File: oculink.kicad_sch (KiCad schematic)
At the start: 28 parts, among them J4 OCuLink_x4_Amphenol_G14A42121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, U2 MAX3373EEKA+

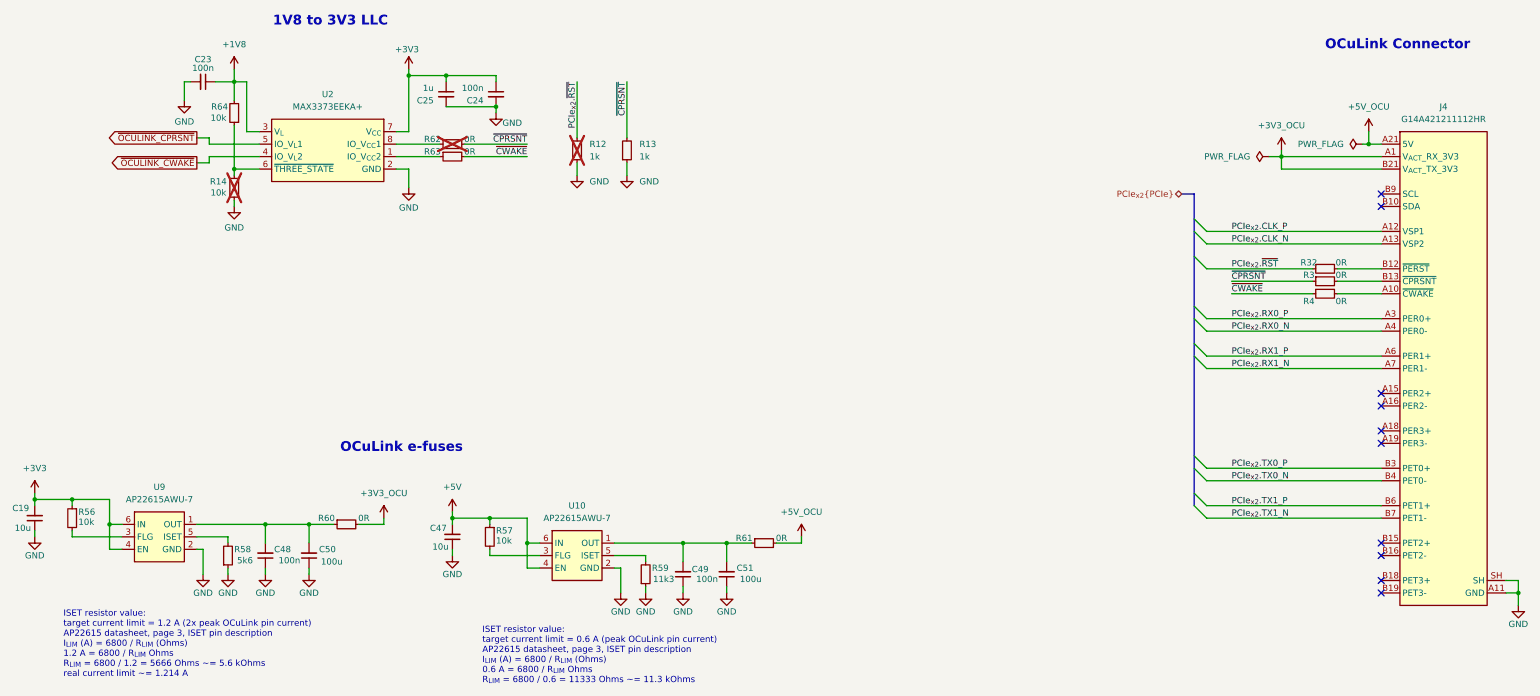
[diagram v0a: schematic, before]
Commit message: [#100765] WIP: Apply review changes
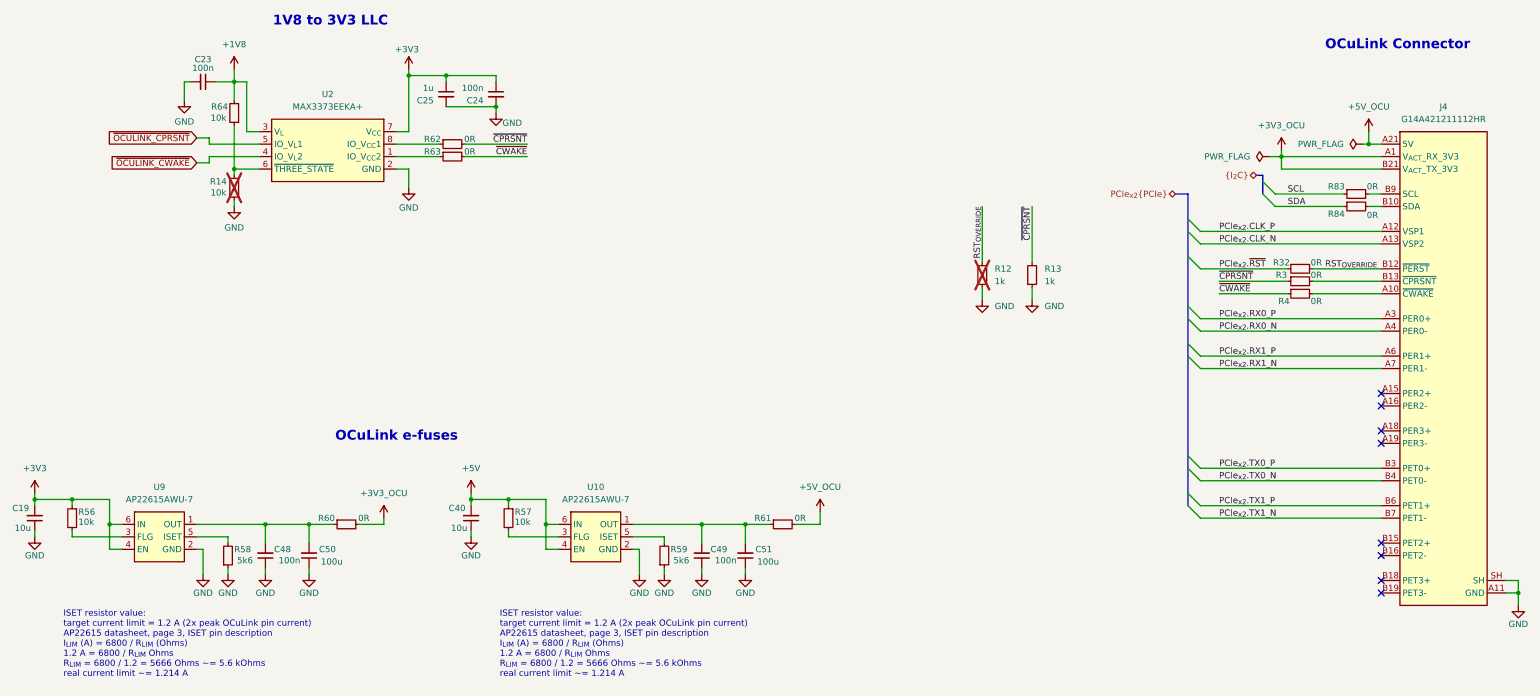
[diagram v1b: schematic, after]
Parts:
- removed C47: C_10u_0402, antmicro-footprints:C_0402_1005Metric, symbol antmicroCapacitors0402:C_10u_0402
- removed R59: R_11k3_0402, antmicro-footprints:R_0402_1005Metric, symbol antmicroResistors0402:R_11k3_0402
- added C40: C_10u_0402, antmicro-footprints:C_0402_1005Metric, symbol antmicroCapacitors0402:C_10u_0402
- added R59: R_5k6_0402, antmicro-footprints:R_0402_1005Metric, symbol antmicroResistors0402:R_5k6_0402
- added R83, R84: R_0R_0402, antmicro-footprints:R_0402_1005Metric, symbol antmicroResistors0402:R_0R_0402
- R62: now fitted
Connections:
- net +5V: now also C40.2
- net GND: now also C40.1, R59.1
- net PCIe_{x2}.~{RST}: no longer R12.2
- net at U10.5 (ISET): now also R59.2
- net RST_{OVERRIDE}: now reaches J4.B12 (~{PERST}), R32.2
- net RST_{OVERRIDE}: now also R12.2
- net at J4.B10 (SDA): now also R84.2
- net at J4.B9 (SCL): now also R83.2
- new net SCL: R83.1
- new net SDA: R84.1
- no-connect marks 10 -> 8
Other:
- note removed: "ISET resistor value: target current limit = 0.6 A (peak OCuLink pin current) AP22615 datasheet, page 3, ISET pin description I_{LIM} (A) = 6800 / R_{LIM} (Ohms) 0.6 A = 6800 / R_{LIM} Ohms R_{LIM} = 6800 / 0.6 = 11333 Ohms ~= 11.3 kOhms"
- moved on the sheet: R12, R13, R3, R32, R4

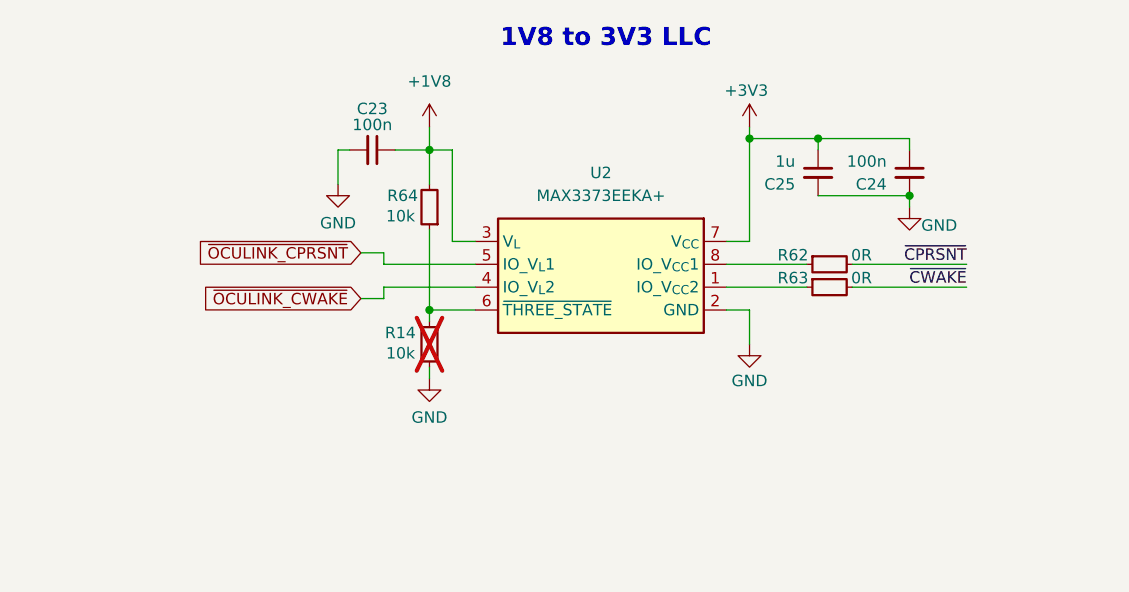
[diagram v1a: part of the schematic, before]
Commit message: [#100765] Change MAX3373EEKA+ to NTS0302JKZ
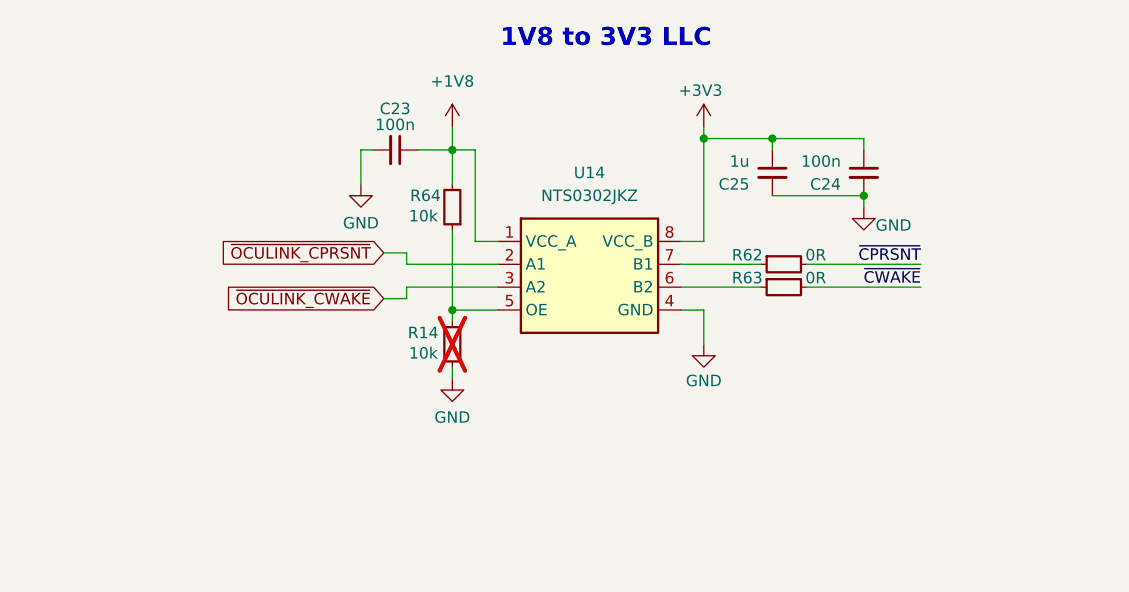
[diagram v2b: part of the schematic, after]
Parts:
- removed U2: MAX3373EEKA+, antmicro-footprints:SOT-23-8, symbol antmicroLogicTranslatorsLevelShifters:MAX3373EEKA+
- added U14: NTS0302JKZ, antmicro-footprints:X2SON8_1.4x1x0.32mm_P0.35mm, symbol antmicroLogicTranslatorsLevelShifters:NTS0302JKZ
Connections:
- net +1V8: now also U14.1 (VCC_A)
- net +3V3: now also U14.8 (VCC_B)
- net GND: now also U14.4 (GND)
- net ~{OCULINK_CPRSNT}: now also U14.2 (A1)
- net ~{OCULINK_CWAKE}: now also U14.3 (A2)
- net at R14.2, R64.1: now also U14.5 (OE)
- net at R63.1: now also U14.6 (B2)
- net at R62.1: now also U14.7 (B1)
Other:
- moved on the sheet: C23, C24, C25, R14, R62, R63, R64

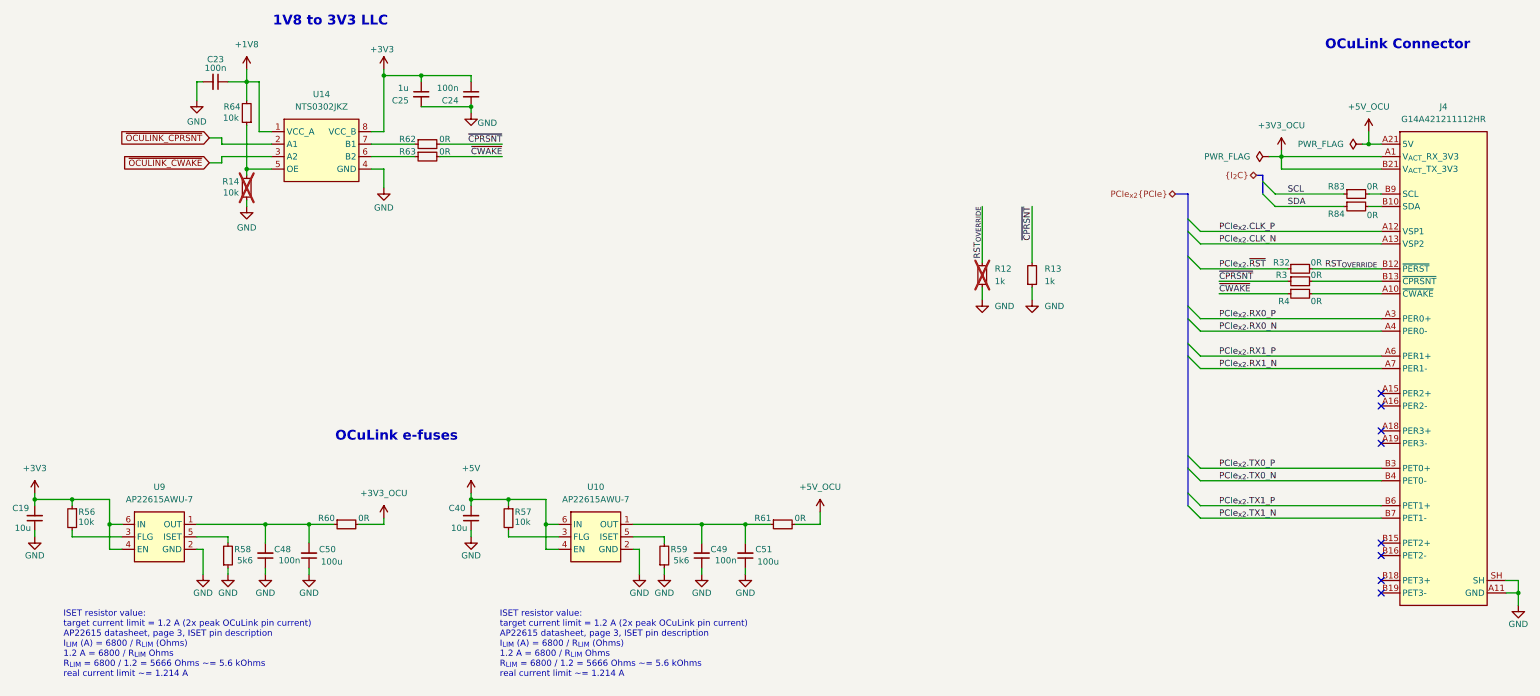
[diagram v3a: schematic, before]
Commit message: [#100765] Reset designators
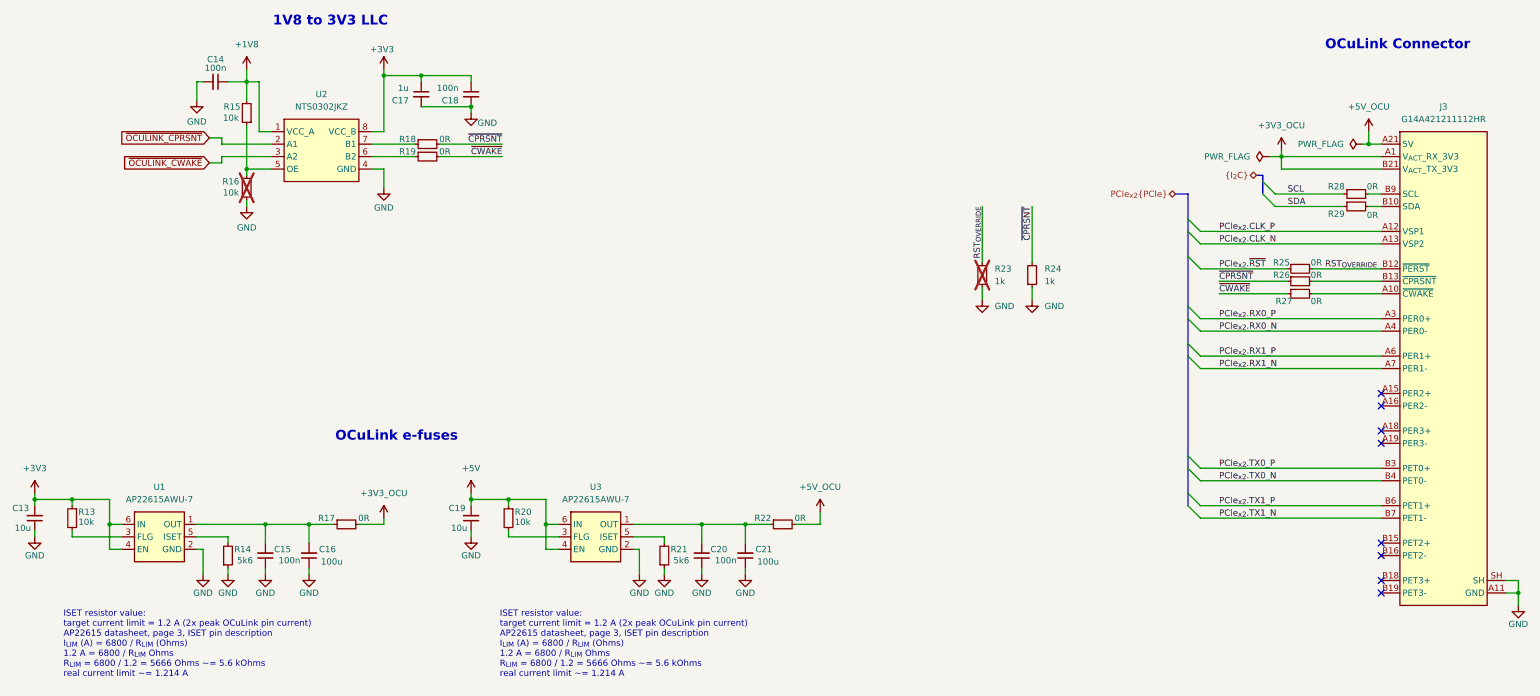
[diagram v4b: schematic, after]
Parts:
- renumbered C19 to C13, C23 to C14, C48 to C15, C50 to C16, C25 to C17, C24 to C18, C40 to C19, C49 to C20, C51 to C21, J4 to J3, R56 to R13, R58 to R14, R64 to R15, R14 to R16, R60 to R17, R62 to R18, R63 to R19, R57 to R20, R59 to R21, R61 to R22, R12 to R23, R13 to R24, R32 to R25, R3 to R26, R4 to R27, R83 to R28, R84 to R29, U9 to U1, U14 to U2, U10 to U3

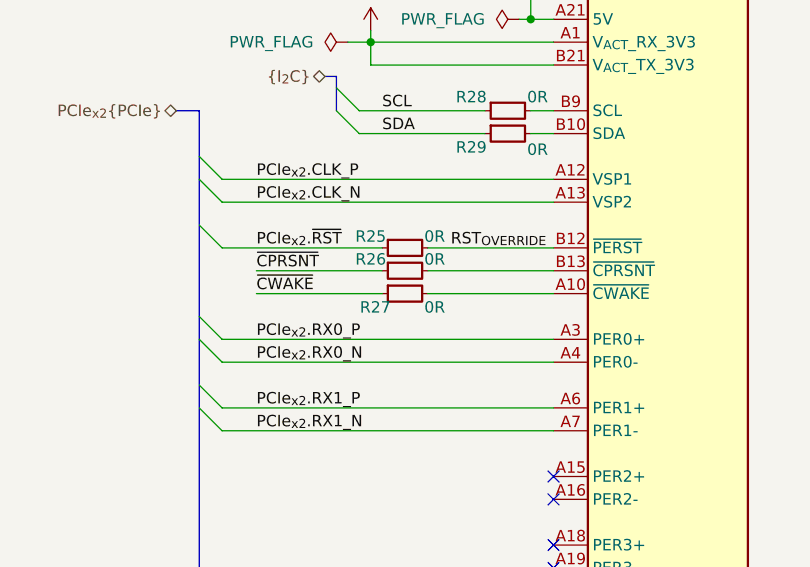
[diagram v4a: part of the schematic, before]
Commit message: [#101557] Remove obsolete 0R on CWAKE# and CPRSNT#
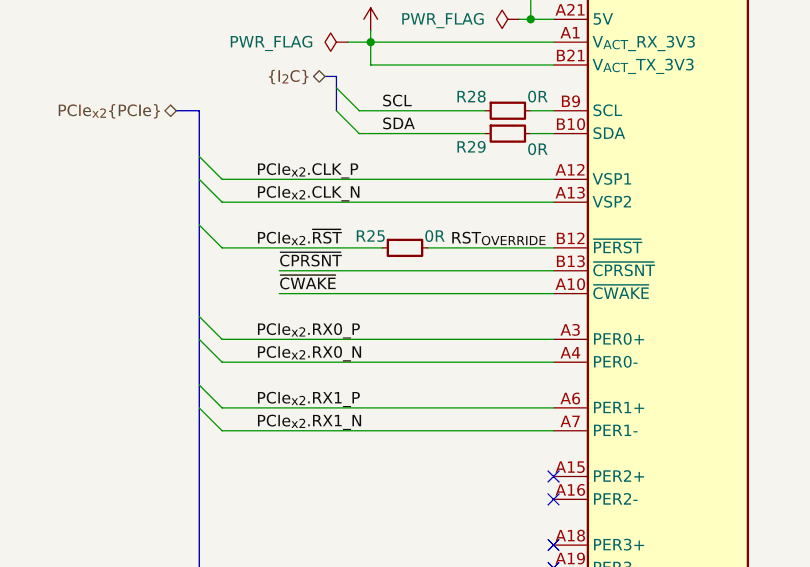
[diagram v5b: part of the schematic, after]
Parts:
- removed R26, R27: R_0R_0402, antmicro-footprints:R_0402_1005Metric, symbol antmicroResistors0402:R_0R_0402
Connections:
- net ~{CPRSNT}: now also J3.B13 (~{CPRSNT})
- net ~{CWAKE}: now also J3.A10 (~{CWAKE})

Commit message: [#101557] Replace 0402 0R to 0R_22.4A
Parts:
- removed R17, R22: R_0R_0402, antmicro-footprints:R_0402_1005Metric, symbol antmicroResistors0402:R_0R_0402
- added R138, R27: R_0R_22.4A_0603, antmicro-footprints:R_0603_1608Metric, symbol antmicroResistors0603:R_0R_22.4A_0603
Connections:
- net +3V3_OCU: now also R138.2
- net +5V_OCU: now also R27.2
- net at C20.2, C21.2, U3.1 (OUT): now also R27.1
- net at C15.2, C16.2, U1.1 (OUT): now also R138.1
